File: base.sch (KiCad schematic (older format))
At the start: 33 parts, among them J1 USB_B_Mini, J10 GPIO, J2 CAN, J3 PWR, J9 UART, P1 SWD, U1 TJA1051TK-3, U2 STM32F40X_LQFP64, U3 MPU9250, Y1 8M

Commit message: some routing
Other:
- note removed: "Temporary!!"
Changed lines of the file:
@@
 EESchema Schematic File Version 4
 LIBS:robot_pcb0-cache
-EELAYER 26 0
+EELAYER 29 0
 EELAYER END
 $Descr A4 11693 8268
@@
 Wire Wire Line
 	3400 4700 3200 4700
-Text Notes 2650 4500 3    50   ~ 0
-Temporary!!
 Text GLabel 3200 4400 0    50   Output ~ 0
 DRV_AIN1_2

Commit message: update
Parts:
- removed C14: 100n, Capacitor_SMD:C_0603_1608Metric, symbol robot_pcb0-rescue:C-device-vesc_hp_v1-rescue-uwb_pcb-rescue
- removed U3: MPU9250, crf1:QFN-24-1EP_3x3mm_P0.4mm_nopp, symbol robot_pcb0-rescue:MPU9250-crf_1
- added U3: BMI160, Package_LGA:Bosch_LGA-14_3x2.5mm_P0.5mm, symbol bmi160:BMI160
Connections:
- net GND: now also U3.1 (SDO), U3.6 (GNDIO), U3.7 (GND)
- net SCL: now also U3.13 (SCx)
- net SDA: now also U3.14 (SDx)
- net VCC: now also U3.12 (CSB), U3.5 (VDDIO), U3.8 (VDD)
- net IMU_INT2: now reaches U2.57 (PB5)
- net IMU_INT2: now also U3.9 (INT2)
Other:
- note added: "Temporary!!"
- moved on the sheet: C15, C16, R4, R5

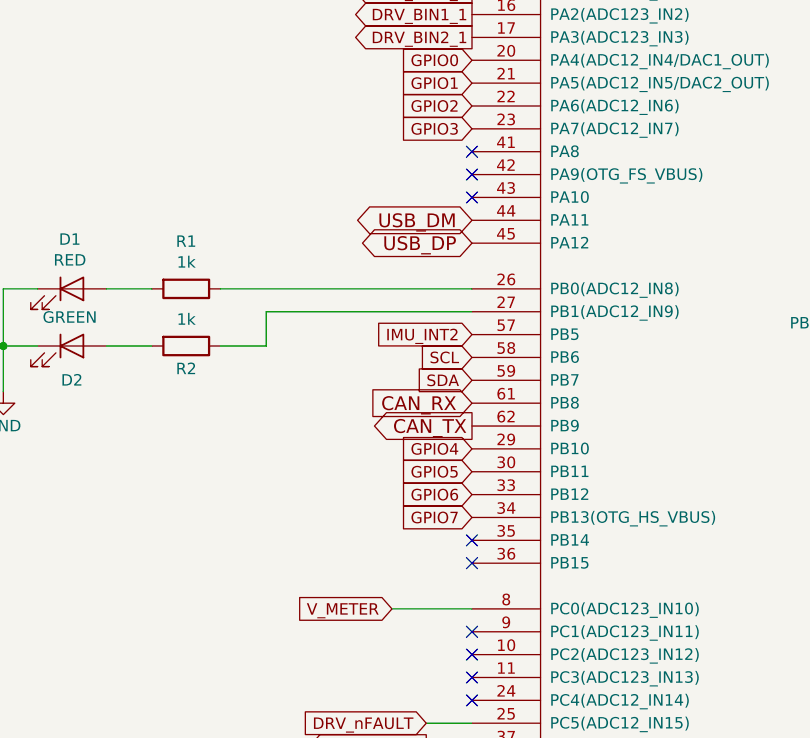
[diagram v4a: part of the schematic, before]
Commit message: adding an nrf52
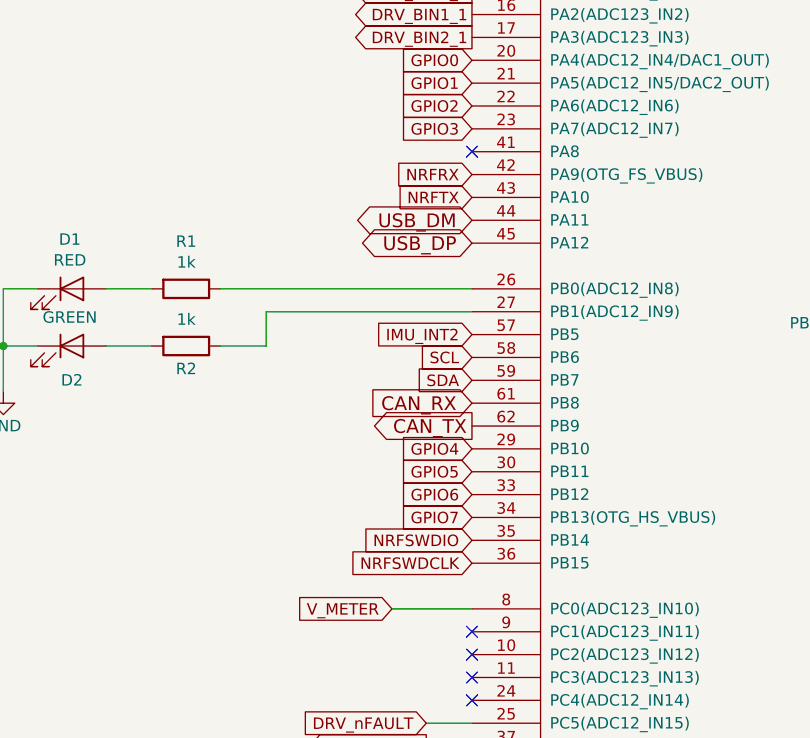
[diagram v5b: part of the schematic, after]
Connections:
- net NRFSWDIO: now reaches U2.35 (PB14)
- net NRFSWDCLK: now reaches U2.36 (PB15)
- net NRFRX: now reaches U2.42 (PA9(OTG_FS_VBUS))
- net NRFTX: now reaches U2.43 (PA10)
- no-connect marks 25 -> 21
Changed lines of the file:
@@
 $Descr A4 11693 8268
 encoding utf-8
-Sheet 2 5
+Sheet 2 6
 Title ""
 Date ""
@@
 Wire Wire Line
 	6150 5350 6200 5350
-Wire Wire Line
-	6150 5200 6150 5350
 Wire Wire Line
 	5900 5200 6150 5200
@@
 	1350 2650 1350 2850
 NoConn ~ 3400 1800
-NoConn ~ 3400 1900
-NoConn ~ 3400 2000
-NoConn ~ 3400 3500
-NoConn ~ 3400 3600
 $Comp
 L power:PWR_FLAG #FLG01
@@
 Wire Wire Line
 	2300 2400 3400 2400
+Wire Wire Line
+	6150 5200 6150 5350
 $Comp
 L robot_pcb0-rescue:STM32F40X_LQFP64-crf_1 U2
@@
 	1    0    0    -1
 $EndComp
+Text GLabel 3400 2000 0    50   Input ~ 0
+NRFTX
+Text GLabel 3400 1900 0    50   Input ~ 0
+NRFRX
+Text GLabel 3400 3500 0    50   Input ~ 0
+NRFSWDIO
+Text GLabel 3400 3600 0    50   Input ~ 0
+NRFSWDCLK
 $EndSCHEMATC

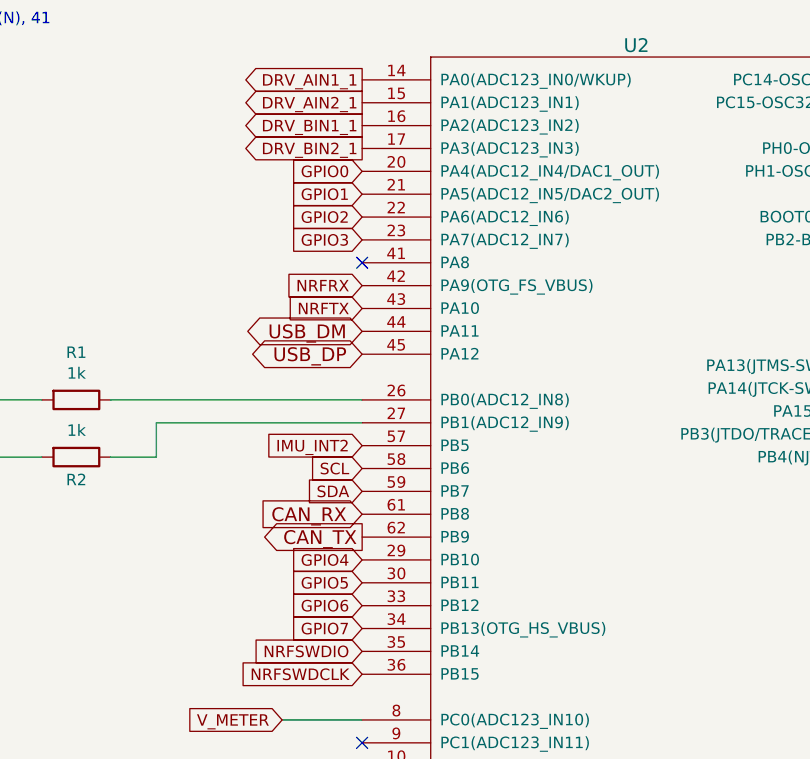
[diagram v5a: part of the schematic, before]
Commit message: Routing done with nrf52
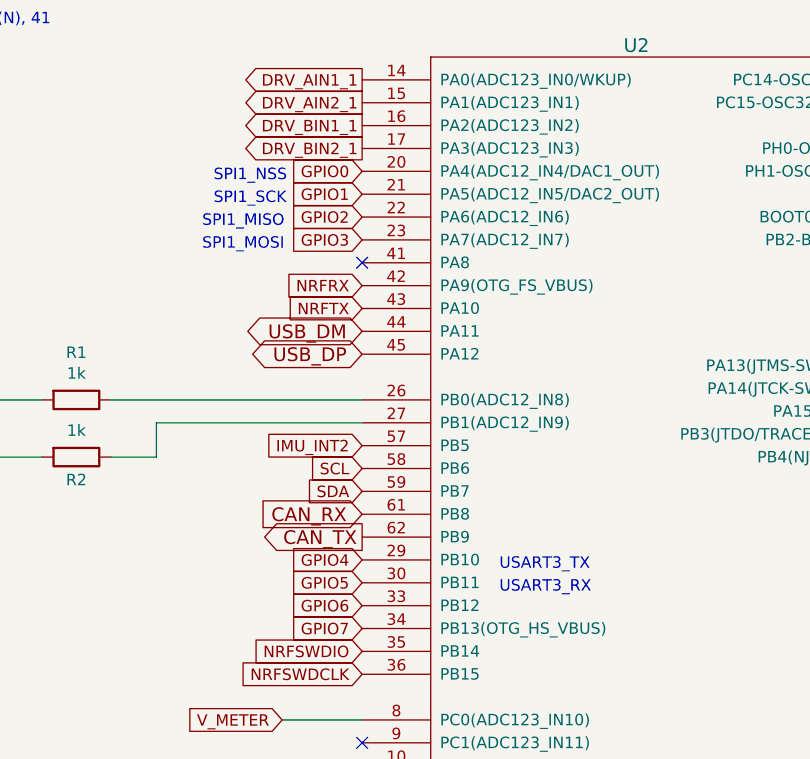
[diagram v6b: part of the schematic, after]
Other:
- note added: "SPI1_MISO\n"
- note added: "SPI1_MOSI"
- note added: "SPI1_NSS\n"
- note added: "SPI1_SCK"
- note added: "USART3_RX\n"
- note added: "USART3_TX\n"
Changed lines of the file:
@@
 Wire Wire Line
 	1500 2650 1350 2650
-Wire Wire Line
-	1350 2650 1350 2850
 NoConn ~ 3400 1800
 $Comp
@@
 NoConn ~ 3400 3900
 Wire Wire Line
-	2500 2500 2500 2650
-Wire Wire Line
 	2500 2650 2300 2650
-Wire Wire Line
-	1350 2400 1350 2650
 Connection ~ 1350 2650
 Text Notes 1700 5700 1    50   ~ 0
@@
 Wire Wire Line
 	3400 3800 3050 3800
-Text Notes 500  2700 0    50   ~ 0
-LQFP64\nTIM 2,3,4,5 PWM\n\n(TIM1 is more capable than TIM2 - 5\nTIM1 CH1 PIN 23 (N), 27(N), 34(N), 36(N), 41\nTIM1 CH2 PIN 42\nTIM1 CH3 PIN 43\nTIM1 CH4 PIN 44\n \n(Maybe prefer these ?) \nTIM2 CH1 PIN 14, 21\nTIM2 CH2 PIN 15, 55\nTIM2 CH3 PIN 16, 29\nTIM2 CH4 PIN 17, 30\n\nTIM3 CH1 PIN 37, 56\nTIM3 CH2 PIN 38 \nTIM3 CH3 PIN 26, 39\nTIM3 CH4 PIN 40 \n\nTIM4 CH1 PIN 58\nTIM4 CH2 PIN 59\nTIM4 CH3 PIN 61\nTIM4 CH4 PIN 62\n\nTIM5 CH1 PIN 14, 22\nTIM5 CH2 PIN 15\nTIM5 CH3 PIN 16\nTIM5 CH4 PIN 17 \n
 $Comp
 L Connector:Conn_01x04_Female J9
@@
 Text GLabel 3400 3600 0    50   Input ~ 0
 NRFSWDCLK
+Text Notes 4000 3150 0    50   ~ 0
+USART3_TX\n
+Text Notes 4000 3250 0    50   ~ 0
+USART3_RX\n
+Text Notes 2750 1450 0    50   ~ 0
+SPI1_NSS\n
+Text Notes 2750 1550 0    50   ~ 0
+SPI1_SCK
+Text Notes 2700 1650 0    50   ~ 0
+SPI1_MISO\n
+Text Notes 2700 1750 0    50   ~ 0
+SPI1_MOSI
+Text Notes 500  2700 0    50   ~ 0
+LQFP64\nTIM 2,3,4,5 PWM\n\n(TIM1 is more capable than TIM2 - 5\nTIM1 CH1 PIN 23 (N), 27(N), 34(N), 36(N), 41\nTIM1 CH2 PIN 42\nTIM1 CH3 PIN 43\nTIM1 CH4 PIN 44\n \n(Maybe prefer these ?) \nTIM2 CH1 PIN 14, 21\nTIM2 CH2 PIN 15, 55\nTIM2 CH3 PIN 16, 29\nTIM2 CH4 PIN 17, 30\n\nTIM3 CH1 PIN 37, 56\nTIM3 CH2 PIN 38 \nTIM3 CH3 PIN 26, 39\nTIM3 CH4 PIN 40 \n\nTIM4 CH1 PIN 58\nTIM4 CH2 PIN 59\nTIM4 CH3 PIN 61\nTIM4 CH4 PIN 62\n\nTIM5 CH1 PIN 14, 22\nTIM5 CH2 PIN 15\nTIM5 CH3 PIN 16\nTIM5 CH4 PIN 17 \n
+Wire Wire Line
+	1350 2400 1350 2650
+Wire Wire Line
+	2500 2500 2500 2650
+Wire Wire Line
+	1350 2650 1350 2850
 $EndSCHEMATC
